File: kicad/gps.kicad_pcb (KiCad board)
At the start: 2 copper layers, 84.1 x 61.7 mm, 84 parts, among them J1 Bus_PCI_Express_x1, J2 USB_C_Receptacle_USB2.0_16P, J3 Conn_01x02, U2 W25Q128JVP, U3 MCP25625T-E/ML, U4 RP2040, U5 NEO-M9N, U6 USB2514B-AEZC-TR, X1 ABM8-272-T3, X2 24MHz, Y1 X322516MLB4SI

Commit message: Update pcb
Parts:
- moved D2 124.2 mm to (134.7, 149.2)
- moved PPS_LED1 124.2 mm to (130.5, 144.3)
- moved PWR1 124.2 mm to (130.5, 147.5)
- moved R1 124.2 mm to (139.2, 130.1)
- moved R18 124.2 mm to (145.0, 130.1)
- moved R19 124.2 mm to (145.0, 132.1)
- moved R2 124.2 mm to (139.2, 132.1)
- moved R21 124.2 mm to (145.0, 136.0)
- moved R23 124.2 mm to (147.9, 130.1)
- moved R25 124.2 mm to (147.9, 132.1)
- moved R29 124.2 mm to (147.9, 136.0)
- moved R4 124.2 mm to (139.2, 136.0)
- moved R5 124.2 mm to (142.1, 130.1)
- moved R6 124.2 mm to (142.1, 132.1)
- moved R9 124.2 mm to (142.1, 136.0)
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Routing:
- net +3.3V: track 103.5 -> 161.6 mm
- net /SWCLK: track 45.9 -> 4.45 mm
- net /SWD: track 41.8 -> 3.52 mm
- net /RUN: track 38.0 -> 8.82 mm, vias 2 -> 1
- net USART4_TX: track 20.2 -> 0.03 mm
- net /QSPI_SS: track 24.4 -> 43.0 mm, vias 0 -> 2
- net USART4_RX: track 18.5 -> 0.00 mm
- net USB_D-: track 13.4 -> 3.85 mm
- net USB_D+: track 13.2 -> 4.08 mm
- net CANN: track 21.1 -> 27.4 mm
- net CANP: track 21.1 -> 27.3 mm
- net +5V: track 52.6 -> 47.4 mm
- net (no net): track 10.1 -> 5.30 mm, vias 1 -> 0
- net +3V3: track 0.00 -> 3.75 mm, vias 0 -> 1
- net /~{USB_BOOT_S}: track 9.32 -> 8.76 mm
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
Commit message: Update pcb
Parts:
- removed C1, C25, C26, C27: 100n, Capacitor_SMD:C_0402_1005Metric
- removed C24, C28, C31: 1u, Capacitor_SMD:C_0402_1005Metric
- removed C29, C30: 12p, Capacitor_SMD:C_0402_1005Metric
- removed D1: LED, LED_SMD:LED_0603_1608Metric
- removed R18, R7: 1k, Resistor_SMD:R_0402_1005Metric
- removed R19, R23, R25, R28: 100k, Resistor_SMD:R_0402_1005Metric
- removed R21, R29, R4: 10k, Resistor_SMD:R_0402_1005Metric
- removed R3: 27, Resistor_SMD:R_0402_1005Metric
- removed R5: 1M, Resistor_SMD:R_0402_1005Metric
- removed R6: 12k, Resistor_SMD:R_0402_1005Metric
- removed U6: USB2514B-AEZC-TR, GPSLIB:QFN36_6X6MC_MCH
- removed X2: 24MHz, GPSLIB:CRYSTAL-SMD_4P-L3.2-W2.5-BL
- added J4: USB_C_Receptacle_USB2.0_16P, Connector_USB:USB_C_Receptacle_Palconn_UTC16-G, F.Cu at (148.0, 117.6)
- R1: value 10k -> 5.1k
- R2: value 27 -> 5.1k
- moved D2 74.2 mm to (173.5, 86.0)
- moved PPS_LED1 69.8 mm to (169.3, 86.3)
- moved PWR1 69.8 mm to (169.3, 89.5)
- moved D6 69.8 mm to (173.1, 88.6)
- moved R9 54.5 mm to (172.5, 90.9)
- moved C7 52.3 mm to (168.9, 92.1)
- moved R20 49.5 mm to (172.5, 92.9)
- moved R2 22.7 mm to (151.1, 112.7)
- moved R1 18.1 mm to (144.6, 112.8)
- moved S2 16.4 mm to (137.2, 118.0)
- moved R8 11.9 mm to (124.0, 100.6)
- moved S1 11.9 mm to (121.8, 106.5)
- moved J2 11.7 mm to (126.3, 117.6)
- moved R11 11.7 mm to (122.9, 112.7)
- moved R12 11.7 mm to (129.4, 112.7)
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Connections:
- R1 pad 1: Net-(U6-OCS_N2) -> GND
- R1 pad 2: +3V3 -> Net-(J4-CC1)
- R16 pad 1: /USBDP_DN4 -> USB_D+
- R17 pad 1: /USBDM_DN4 -> USB_D-
- R2 pad 1: /USBDM_DN1 -> Net-(J4-CC2)
- R2 pad 2: Net-(U5-USB_DM) -> GND
- U5 pad 5: Net-(U5-USB_DM) -> GPS_USB_D-
- U5 pad 6: Net-(U5-USB_DP) -> GPS_USB_D+
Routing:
- net +3.3V: track 161.6 -> 117.7 mm, vias 12 -> 10
- net /QSPI_SS: track 43.0 -> 23.9 mm
- net GPS_USB_D+: track 0.00 -> 4.08 mm
- net GPS_USB_D-: track 0.00 -> 3.85 mm
- net Net-(J4-CC1): track 0.00 -> 3.03 mm
- net Net-(J4-CC2): track 0.00 -> 2.71 mm
- net +5V: track 47.4 -> 49.7 mm, vias 1 -> 2
- net GND: vias 89 -> 88

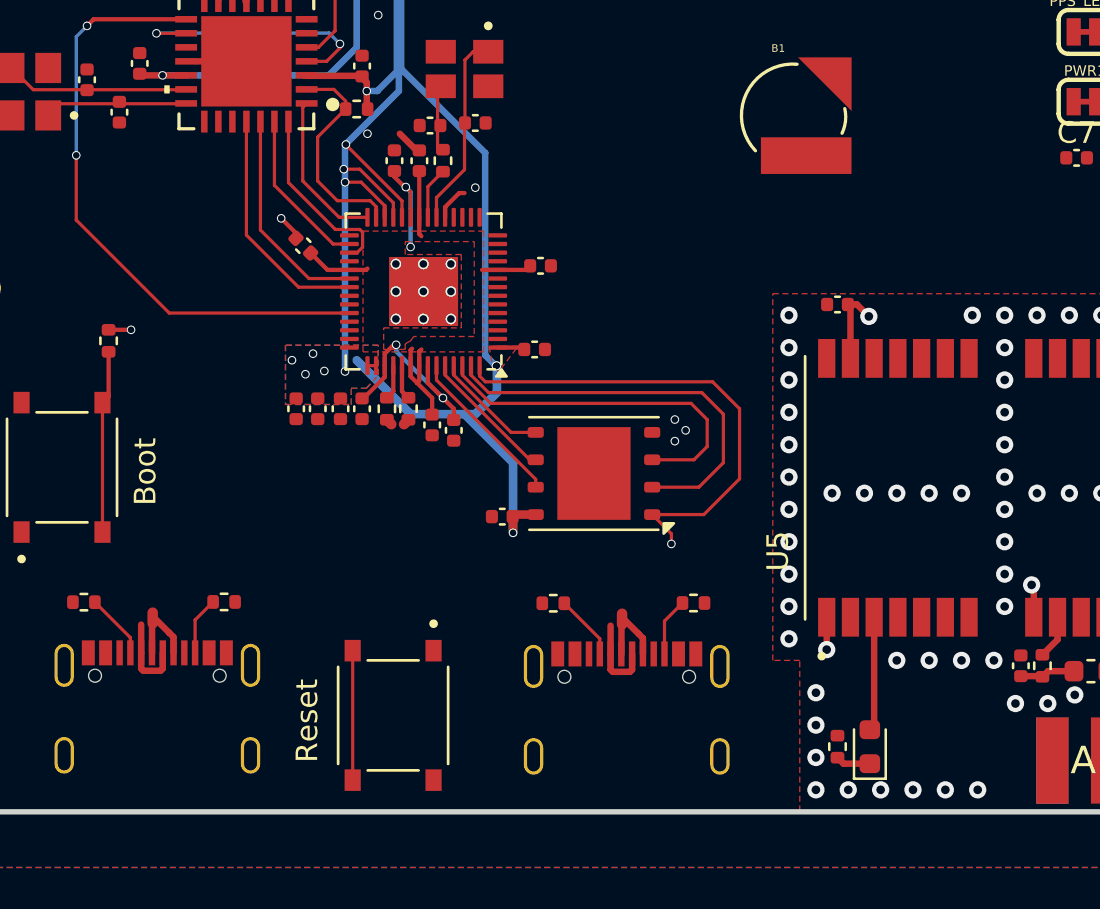
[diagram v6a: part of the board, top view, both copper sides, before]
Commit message: Update gps.kicad_pcb
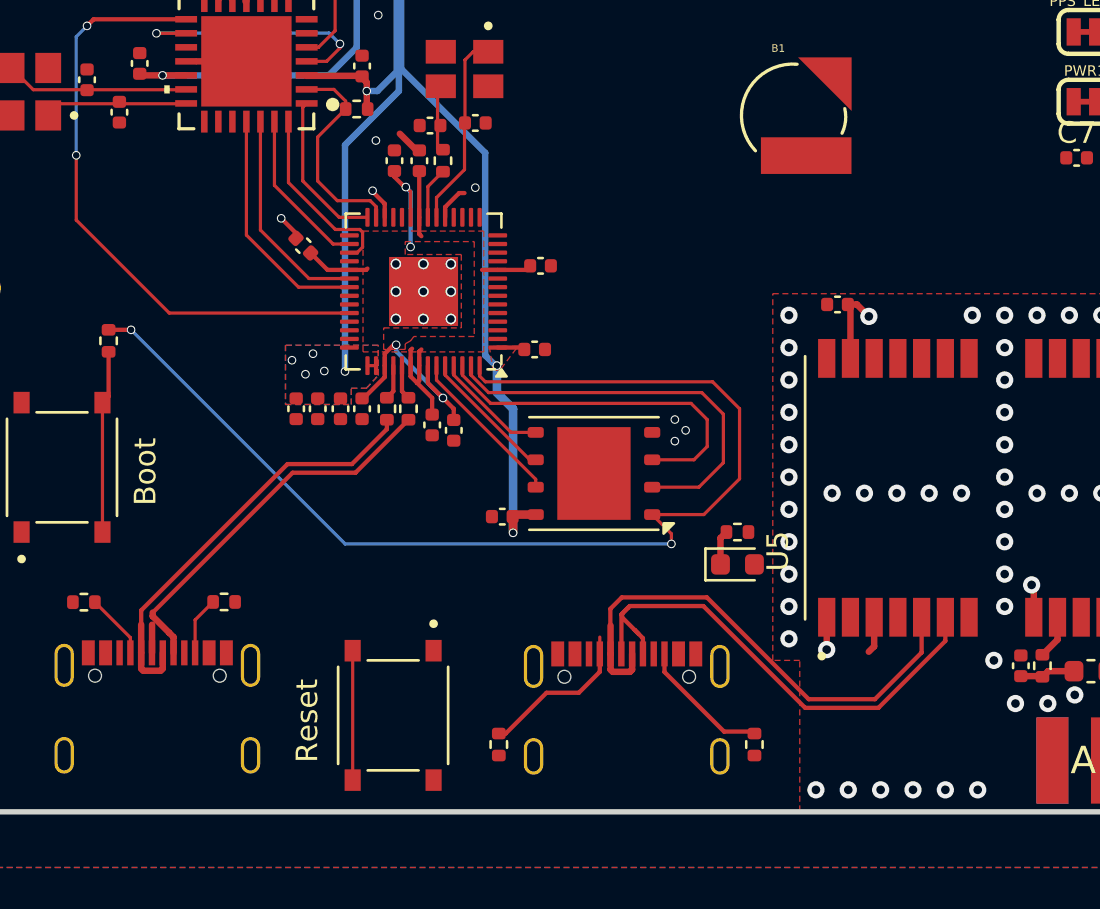
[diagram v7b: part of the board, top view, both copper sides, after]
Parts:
- moved R22 11.0 mm to (153.2, 109.5), turned to 0 degrees
- moved D5 10.4 mm to (153.2, 111.0), turned to 0 degrees
- moved R2 7.14 mm to (153.9, 119.3), turned to -90 degrees
- moved R1 7.02 mm to (142.1, 119.3), turned to 90 degrees
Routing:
- net /QSPI_SS: track 23.9 -> 53.1 mm
- net GPS_USB_D+: track 4.08 -> 24.3 mm
- net GPS_USB_D-: track 3.85 -> 23.8 mm
- net USB_D-: track 4.15 -> 19.8 mm
- net USB_D+: track 4.37 -> 19.1 mm
- net +3.3V: track 117.7 -> 110.1 mm, vias 10 -> 9
- net (no net): track 5.30 -> 0.00 mm
- net /SWCLK: track 4.45 -> 0.00 mm, vias 1 -> 0
- net Net-(J4-CC1): track 3.03 -> 7.47 mm
- net /SWD: track 3.52 -> 0.00 mm, vias 1 -> 0
- net Net-(J4-CC2): track 2.71 -> 6.19 mm
- net /PLS: track 0.00 -> 1.70 mm
- net /RUN: track 8.82 -> 7.44 mm
- net GND: vias 88 -> 82

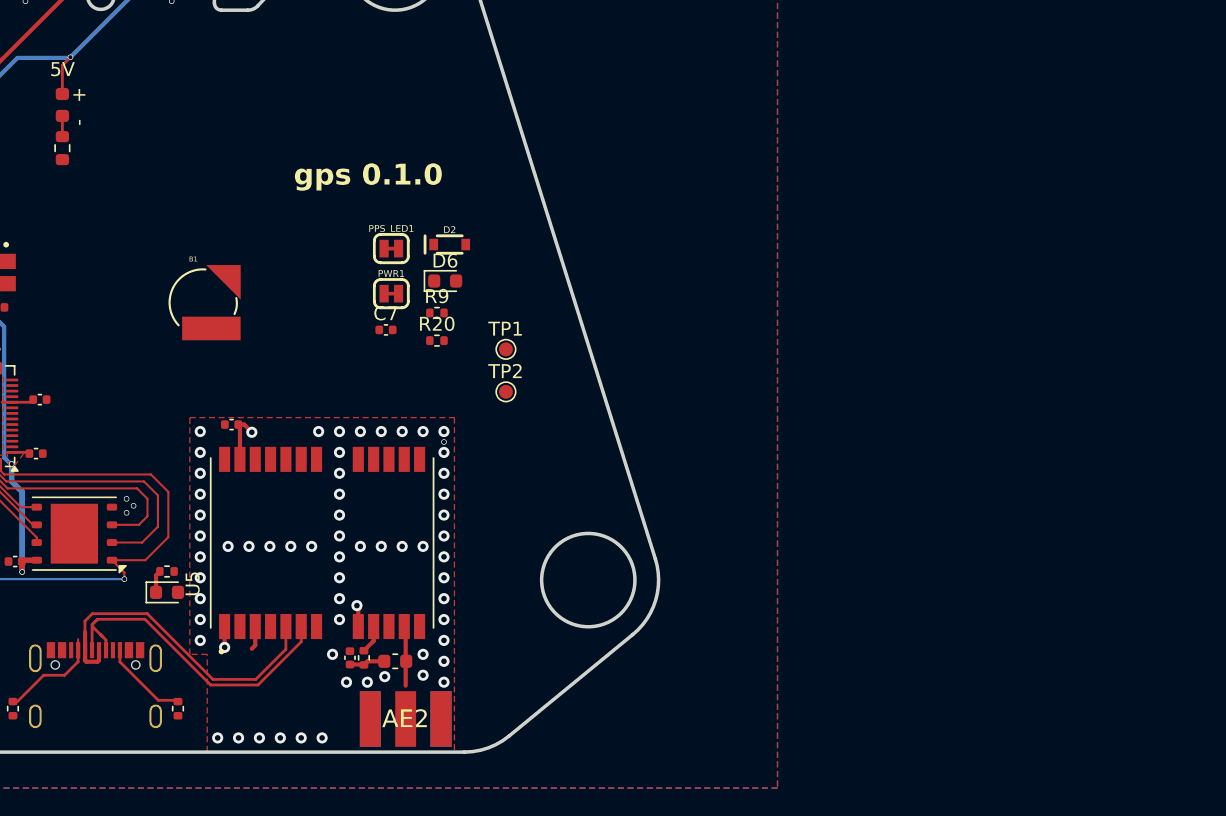
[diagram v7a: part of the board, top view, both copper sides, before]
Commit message: Update gps.kicad_pcb
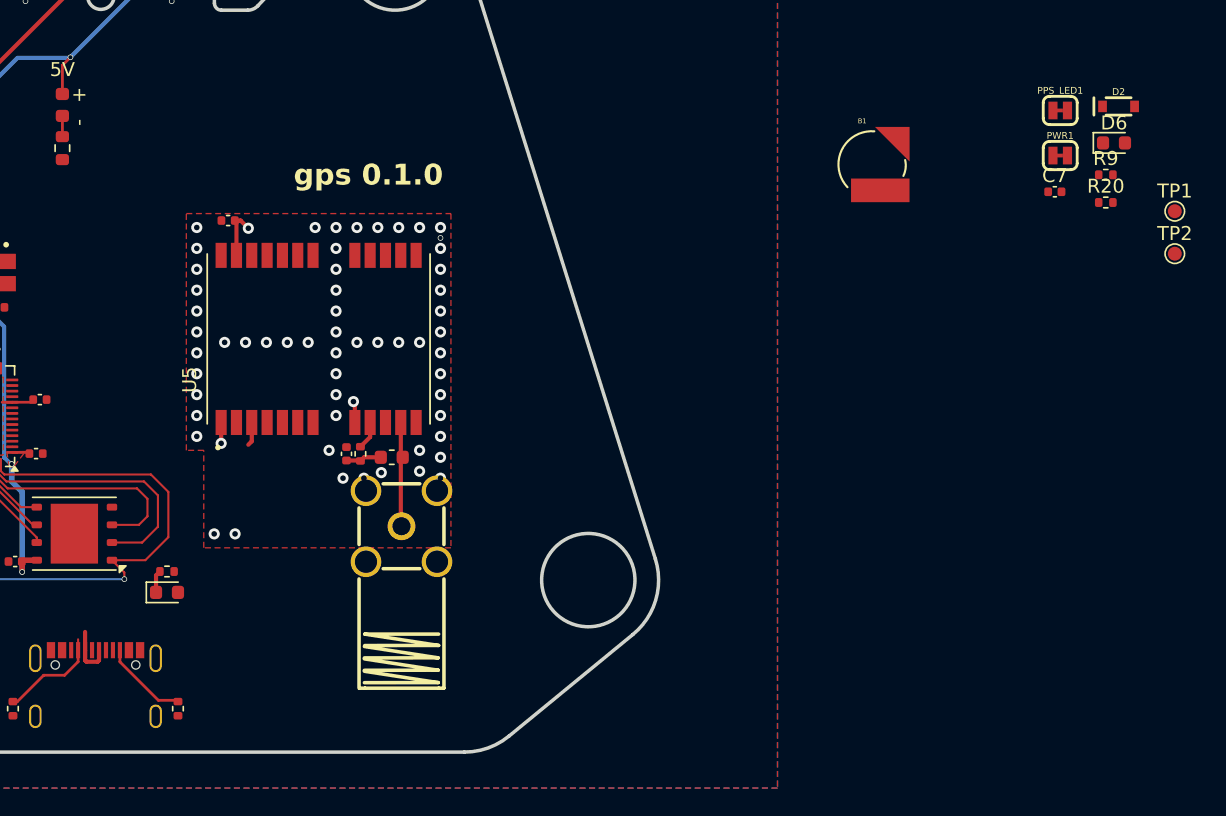
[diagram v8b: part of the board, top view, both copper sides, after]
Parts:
- removed AE2: SMA-M, GPSLIB:SMA-EDGE
- added RF1: BWSMA-KE-P001, GPSLIB:SMA-TH_BWSMA-KWE-Z001, F.Cu at (170.0, 106.2)
- moved C7 49.0 mm to (216.9, 82.2)
- moved D6 49.0 mm to (221.2, 78.7)
- moved B1 49.0 mm to (203.8, 80.2)
- moved D2 49.0 mm to (221.5, 76.1)
- moved PPS_LED1 49.0 mm to (217.3, 76.3)
- moved PWR1 49.0 mm to (217.3, 79.6)
- moved R20 49.0 mm to (220.6, 83.0)
- moved R9 49.0 mm to (220.6, 81.0)
- moved TP1 49.0 mm to (225.5, 83.6)
- moved TP2 49.0 mm to (225.5, 86.6)
- moved C22 14.7 mm to (157.6, 84.2)
- moved C23 14.7 mm to (166.1, 101.0)
- moved L1 14.7 mm to (169.3, 101.2)
- moved R24 14.7 mm to (167.1, 101.0)
- moved U5 14.7 mm to (164.1, 92.8)
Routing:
- net GPS_USB_D+: track 24.3 -> 0.00 mm
- net GPS_USB_D-: track 23.8 -> 3.85 mm
- net Net-(U5-RF_IN): track 4.29 -> 7.90 mm
- net GND: vias 82 -> 75
